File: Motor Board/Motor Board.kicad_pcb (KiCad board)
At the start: 2 copper layers, 37.5 x 39 mm, 30 parts, among them J1 Programmer, J2 Gecko, J3 Gecko, J4 Conn_01x02_Socket, J5 Conn_01x02_Socket, Q1 BSS316NN, U2 PIC18F26K83, U3 MCP2562, U4 INA180, Y1 12MHz Crystal

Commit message: Push motor
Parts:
- added C6: 10uF, Capacitor_SMD:C_0805_2012Metric_Pad1.18x1.45mm_HandSolder, B.Cu at (180.8, 65.3)
- added C7: 10uF, Capacitor_SMD:C_0805_2012Metric_Pad1.18x1.45mm_HandSolder, B.Cu at (171.0, 62.5)
- added C8: 10uF, Capacitor_SMD:C_0805_2012Metric_Pad1.18x1.45mm_HandSolder, B.Cu at (174.0, 62.5)
- added R10: 1kR, Resistor_SMD:R_0805_2012Metric_Pad1.20x1.40mm_HandSolder, B.Cu at (174.0, 56.8)
- added R8: 10kR, Resistor_SMD:R_0805_2012Metric_Pad1.20x1.40mm_HandSolder, B.Cu at (166.9, 65.0)
- added R9: 1kR, Resistor_SMD:R_0805_2012Metric_Pad1.20x1.40mm_HandSolder, B.Cu at (171.0, 56.8)
- added TP1: 5v TP, TestPoint:TestPoint_Pad_1.5x1.5mm, F.Cu at (162.5, 74.5)
- added TP2: PWM TP, TestPoint:TestPoint_Pad_1.5x1.5mm, F.Cu at (162.5, 78.8)
- added TP3: LIM2 TP, TestPoint:TestPoint_Pad_1.5x1.5mm, F.Cu at (165.5, 74.5)
- added TP4: LIM1 TP, TestPoint:TestPoint_Pad_1.5x1.5mm, F.Cu at (165.5, 78.8)
- C1, C2, C3, R1, R2, R3, R4, R6, R7: moved to B.Cu
- F1: value Polyfuse 350mA -> Polyfuse 750mA
- R5: value 62mR -> 10R; moved to B.Cu
- U3, U4, Y1: moved to F.Cu
- moved C1 58.4 mm to (177.7, 55.2), turned to -90 degrees
- moved C2 57.1 mm to (180.8, 55.2), turned to -90 degrees
- moved R2 55.7 mm to (172.8, 49.0), turned to 180 degrees
- moved R1 52.8 mm to (172.8, 45.8), turned to 180 degrees
- moved J4 52.4 mm to (182.0, 48.0)
- moved D2 50.2 mm to (172.8, 45.8), turned to 0 degrees
- moved C3 48.1 mm to (177.7, 60.2), turned to -90 degrees
- moved R5 46.1 mm to (166.9, 60.0), turned to -90 degrees
- moved Y1 45.5 mm to (182.0, 72.5)
- moved R3 43.6 mm to (164.0, 55.0), turned to -90 degrees
- moved R4 43.6 mm to (166.9, 55.0), turned to -90 degrees
- moved R7 43.0 mm to (163.9, 65.0)
- moved Q1 41.6 mm to (172.8, 53.0), turned to 180 degrees
- moved J2 41.4 mm to (186.0, 58.5)
- moved D1 40.9 mm to (172.8, 42.5)
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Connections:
- J3 pad 5: +5V -> Net-(J3-Pin_5)
- J4 pad 1: /LIM_2 -> GND
- J4 pad 2: +5V -> Net-(J4-Pin_2)
- J5 pad 1: /LIM_1 -> GND
- J5 pad 2: +5V -> Net-(J5-Pin_2)
- Q1 pad 2: GND -> +5V
- Q1 pad 3: +5V -> Net-(J3-Pin_5)
- R6 pad 1: /LIM_1 -> +5V
- R6 pad 2: GND -> Net-(J5-Pin_2)
- R7 pad 1: /LIM_2 -> +5V
- R7 pad 2: GND -> Net-(J4-Pin_2)
- U3 pad 2: GND -> Net-(U3-STBY)
- U3 pad 8: GND -> Net-(U3-STBY)
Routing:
- net GND: track 81.2 -> 0.00 mm, vias 6 -> 0
- net Net-(D1-K): track 50.2 -> 0.00 mm, vias 4 -> 0
- net /LIM_1: track 42.4 -> 0.00 mm, vias 2 -> 0
- net /LIM_2: track 40.6 -> 0.00 mm
- net Net-(D2-K): track 38.8 -> 0.00 mm, vias 2 -> 0
- net Net-(D3-K): track 33.1 -> 0.00 mm, vias 2 -> 0
- net +5V: track 31.2 -> 0.00 mm
- net Net-(U4-IN+): track 28.0 -> 0.00 mm, vias 3 -> 0
- net /OSC2: track 28.0 -> 0.00 mm, vias 1 -> 0
- net /OSC1: track 26.5 -> 0.00 mm, vias 1 -> 0
- net Net-(J2-Pin_5): track 20.9 -> 0.00 mm
- net /CANL: track 19.4 -> 0.00 mm, vias 1 -> 0
- net /CANH: track 17.8 -> 0.00 mm, vias 1 -> 0
- net Net-(U2-RA2): track 10.3 -> 0.00 mm
- net /MTR_ON: track 9.39 -> 0.00 mm, vias 1 -> 0
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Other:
- board size 37.5 x 39 mm -> 40 x 40 mm
- board text removed: "CANBUS"
- board text removed: "SERVO"

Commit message: Fix review items
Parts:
- C4, C5, Q1, R1, R2, R3, R4, R6, R7, R8: moved to F.Cu
- F1: value Polyfuse 750mA -> Polyfuse 1.5A
- R5: value 10R -> 50mR
- U3, U4: moved to B.Cu
- moved TP3 30.1 mm to (181.5, 49.0)
- moved TP2 28.2 mm to (171.5, 52.0)
- moved R7 27.4 mm to (181.5, 44.0), turned to 0 degrees
- moved TP4 27.0 mm to (190.0, 67.5)
- moved C6 26.6 mm to (154.5, 69.8)
- moved F1 26.1 mm to (174.5, 68.5), turned to -90 degrees
- moved D1 26.0 mm to (154.5, 61.0), turned to 90 degrees
- moved R1 24.9 mm to (163.2, 68.8), turned to 0 degrees
- moved R2 24.8 mm to (154.5, 65.8), turned to -90 degrees
- moved C2 24.3 mm to (161.2, 69.8)
- moved J5 23.9 mm to (185.6, 61.0), turned to 90 degrees
- moved C1 23.7 mm to (159.0, 69.8)
- moved C3 23.0 mm to (156.8, 69.8), turned to 90 degrees
- moved J2 22.8 mm to (169.2, 74.0), turned to 0 degrees
- moved R6 22.1 mm to (185.5, 65.0), turned to 0 degrees
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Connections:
- C4 pad 2: Net-(C4-Pad2) -> GND
- C5 pad 2: Net-(C4-Pad2) -> GND
- J3 pad 4: /MTR_OUT -> unconnected-(J3-Pin_4-Pad4)
- J4 pad 1: GND -> Net-(J4-Pin_1)
- J4 pad 2: Net-(J4-Pin_2) -> +5V
- J5 pad 1: GND -> Net-(J5-Pin_1)
- J5 pad 2: Net-(J5-Pin_2) -> +5V
- R10 pad 1: GND -> Net-(J5-Pin_1)
- R6 pad 1: +5V -> /LIM_1
- R6 pad 2: Net-(J5-Pin_2) -> GND
- R7 pad 1: +5V -> /LIM_2
- R7 pad 2: Net-(J4-Pin_2) -> GND
- R9 pad 1: GND -> Net-(J4-Pin_1)
- U2 pad 25: /MTR_OUT -> unconnected-(U2-RB4-Pad25)
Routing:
- net GND: track 0.00 -> 92.3 mm, vias 0 -> 1
- net +5V: track 0.00 -> 72.5 mm, vias 0 -> 1
- net /LIM_2: track 0.00 -> 24.8 mm, vias 0 -> 1
- net Net-(U2-RA2): track 0.00 -> 19.3 mm
- net /OSC1: track 0.00 -> 18.6 mm
- net /LIM_1: track 0.00 -> 16.4 mm, vias 0 -> 1
- net Net-(U2-RA1): track 0.00 -> 14.5 mm
- net /CAN_RX: track 0.00 -> 14.1 mm, vias 0 -> 1
- net /OSC2: track 0.00 -> 13.8 mm
- net /MTR_IN: track 0.00 -> 12.2 mm
- net Net-(U2-RA0): track 0.00 -> 11.4 mm
- net Net-(J2-Pin_5): track 0.00 -> 11.0 mm
- net /CANL: track 0.00 -> 10.0 mm
- net /CURR_SENS: track 0.00 -> 9.87 mm, vias 0 -> 1
- net /CANH: track 0.00 -> 9.67 mm
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
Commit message: Forgot to push, fix mosfets
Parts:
- added C1: 0.1uF, Capacitor_SMD:C_0805_2012Metric_Pad1.18x1.45mm_HandSolder, B.Cu at (178.4, 59.4)
- added Q2: DMG2305UX-7, Package_TO_SOT_SMD:SOT-23, B.Cu at (171.1, 53.1)
- added R11: 10kR, Resistor_SMD:R_0805_2012Metric_Pad1.20x1.40mm_HandSolder, B.Cu at (166.8, 55.2)
- added R12: 120R, Resistor_SMD:R_0805_2012Metric_Pad1.20x1.40mm_HandSolder, B.Cu at (167.6, 59.2)
- added R8: 10kR, Resistor_SMD:R_0805_2012Metric_Pad1.20x1.40mm_HandSolder, B.Cu at (176.6, 54.0)
- Q1: footprint Package_TO_SOT_SMD:SOT-323_SC-70 -> Package_TO_SOT_SMD:SOT-323_SC-70_Handsoldering
- moved Q1 0.37 mm to (167.7, 52.0), turned to 0 degrees
- renumbered C3 to C2, C4 to C3, C5 to C4, C6 to C5, C7 to C6, C8 to C7
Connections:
- Q1 pad 1: /MTR_ON -> Net-(Q1-G)
- Q1 pad 2: +5V -> GND
- Q1 pad 3: Net-(J3-Pin_5) -> Net-(Q1-D)
- U3 pad 2: Net-(U3-STBY) -> GND
- U3 pad 8: Net-(U3-STBY) -> GND
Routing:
- net +5V: track 72.5 -> 89.8 mm
- net Net-(Q1-D): track 0.00 -> 13.6 mm, vias 0 -> 1
- net GND: track 92.3 -> 103.6 mm
- net Net-(Q1-G): track 0.00 -> 10.7 mm, vias 0 -> 1
- net Net-(U3-STBY): track 5.48 -> 0.00 mm
- net /MTR_ON: track 6.76 -> 10.4 mm, vias 0 -> 1
- net Net-(J3-Pin_5): track 7.16 -> 10.4 mm
- net /MTR_IN: track 12.2 -> 14.7 mm
- net /ICSPDAT: track 4.25 -> 3.25 mm
- net /ICSPCLK: track 6.13 -> 6.80 mm

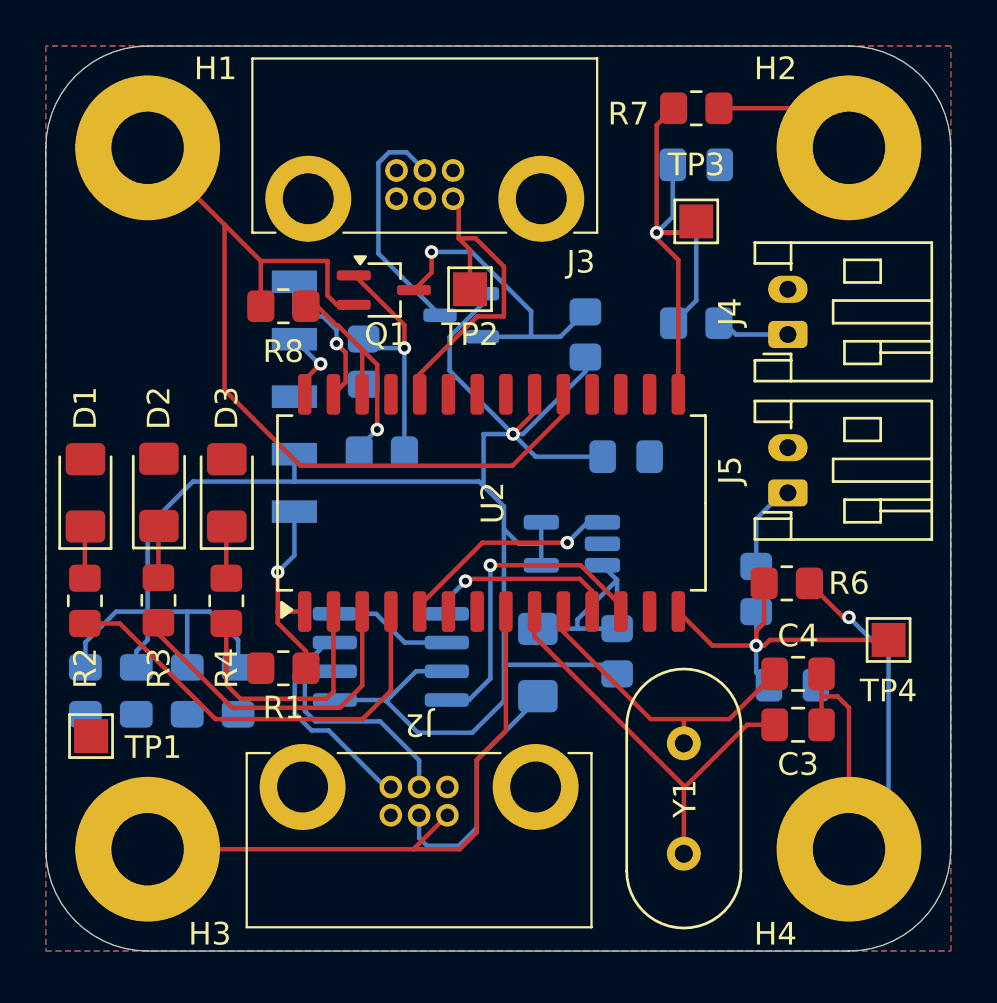
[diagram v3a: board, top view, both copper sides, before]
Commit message: Fix the traces and comments from Pranav
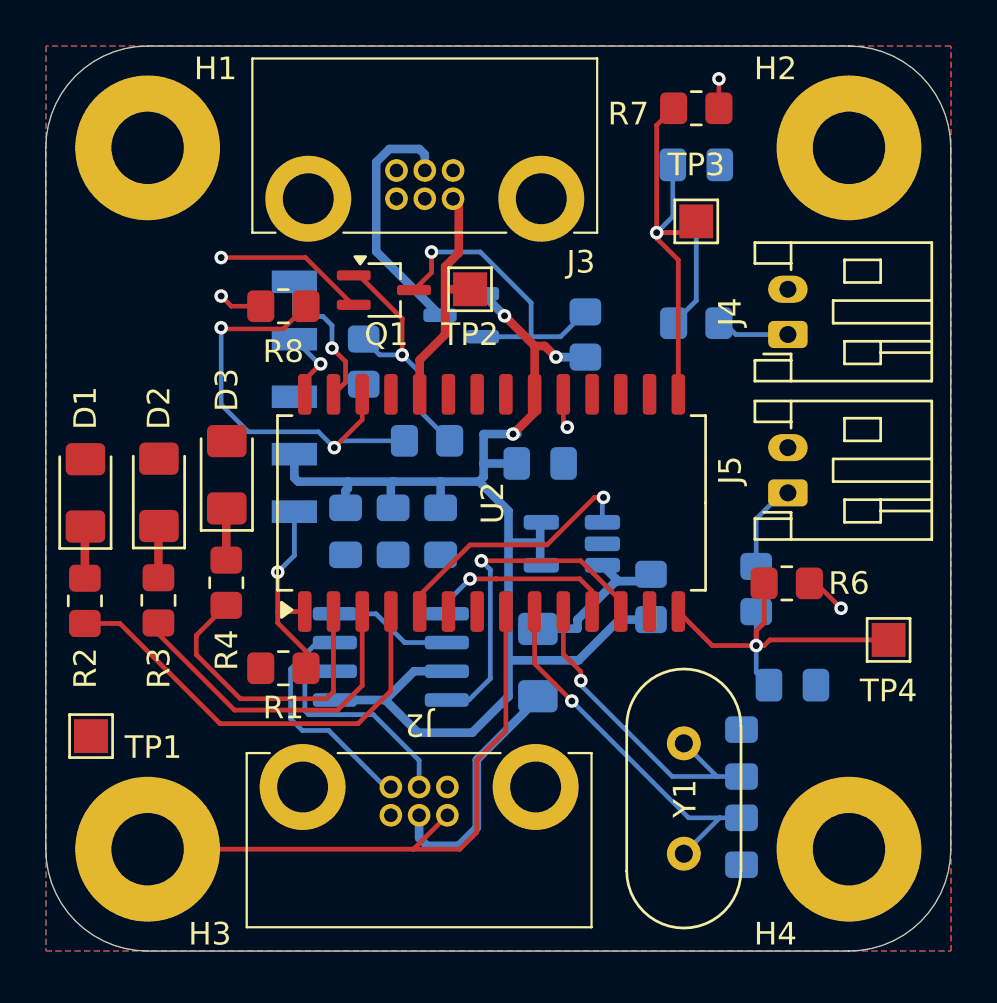
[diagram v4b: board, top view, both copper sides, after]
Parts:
- removed the C2 at (161.2, 69.8)
- C3, C4: moved to B.Cu
- moved C2 20.5 mm to (174.6, 59.7), turned to 180 degrees
- moved C5 13.5 mm to (166.0, 62.7)
- moved C1 11.5 mm to (168.1, 62.7)
- moved C1 8.84 mm to (170.2, 62.7), turned to -90 degrees
- moved C3 5.72 mm to (183.5, 76.4), turned to -90 degrees
- moved C4 4.30 mm to (183.5, 72.5), turned to 90 degrees
- moved R5 2.83 mm to (179.5, 65.6)
- moved R12 2.06 mm to (169.6, 58.7)
- moved D3 0.80 mm to (160.8, 60.2)
- moved R4 0.80 mm to (160.7, 65.0)
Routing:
- net GND: track 103.6 -> 46.1 mm, vias 1 -> 5
- net +5V: track 89.8 -> 60.8 mm, vias 1 -> 3
- net /MTR_ON: track 10.4 -> 19.5 mm, vias 1 -> 2
- net /MTR_IN: track 14.7 -> 10.6 mm
- net Net-(U4-IN+): track 9.45 -> 7.19 mm
- net /OSC1: track 18.6 -> 16.5 mm, vias 0 -> 1
- net Net-(U2-RA0): track 11.4 -> 13.3 mm
- net /CURR_SENS: track 9.87 -> 11.8 mm
- net /OSC2: track 13.8 -> 15.3 mm, vias 0 -> 1
- net /CAN_RX: track 14.1 -> 15.1 mm
- net Net-(J3-Pin_5): track 10.4 -> 11.1 mm
- net /CANH: track 9.67 -> 10.3 mm
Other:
- board text added: "MCLR"

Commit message: redit layout
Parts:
- removed the C1 at (168.1, 62.7)
- removed the C1 at (170.2, 62.7)
- removed the R8 at (163.2, 52.8)
- removed the R8 at (176.6, 54.0)
- added C1: 0.1uF, Capacitor_SMD:C_0805_2012Metric_Pad1.18x1.45mm_HandSolder, F.Cu at (176.9, 63.2)
- added G***: LOGO, Team_Logo:Logo_Horizontal_Silkscreen_10mm, B.Cu at (174.5, 67.8)
- added R8: 10kR, Resistor_SMD:R_0805_2012Metric_Pad1.20x1.40mm_HandSolder, B.Cu at (169.2, 55.5)
- C2, C3, C4, C5, C6, C7, F1, R10, R5, R9, U3, U4: moved to F.Cu
- J1: footprint Canhw:PinSocket_5x2.54_SMD_90deg_952-3198-1-ND -> canhw:PinSocket_5x2.54_SMD_90deg_952-3198-1-ND
- J2, J3: footprint Canhw:connector_Harwin_G125–MG10605M4P -> canhw:connector_Harwin_G125–MG10605M4P
- Q1, R1: moved to B.Cu
- Y1: value 12MHz Crystal -> 12MHz Crystal
- moved TP1 38.2 mm to (180.0, 43.1), turned to 180 degrees
- moved C3 30.7 mm to (155.2, 64.5), turned to 90 degrees
- moved C4 28.5 mm to (155.2, 68.8), turned to -90 degrees
- moved Y1 25.2 mm to (159.3, 64.1), turned to -90 degrees
- moved C2 19.6 mm to (191.3, 70.0), turned to -90 degrees
- moved R4 13.2 mm to (161.0, 51.8), turned to 0 degrees
- moved U4 13.1 mm to (187.5, 69.6), turned to -90 degrees
- moved R7 12.1 mm to (179.3, 55.9), turned to -90 degrees
- moved R3 11.4 mm to (161.0, 54.9), turned to 0 degrees
- moved C7 11.1 mm to (179.3, 60.4), turned to 90 degrees
- moved D3 10.4 mm to (155.7, 51.1), turned to 180 degrees
- moved R2 10.2 mm to (161.1, 57.9), turned to 0 degrees
- moved TP2 9.96 mm to (180.0, 46.7)
- moved U3 9.35 mm to (164.6, 77.0), turned to -90 degrees
- moved C5 9.06 mm to (165.6, 71.8), turned to 180 degrees
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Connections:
- U2 pad 14: /LIM_1 -> unconnected-(U2-RC3-Pad14)
- U2 pad 15: /LIM_2 -> unconnected-(U2-RC4-Pad15)
- U2 pad 16: unconnected-(U2-RC5-Pad16) -> /CURR_SENS
- U2 pad 22: unconnected-(U2-RB1-Pad22) -> /LIM_1
- U2 pad 23: unconnected-(U2-RB2-Pad23) -> /LIM_2
- U2 pad 5: /CURR_SENS -> unconnected-(U2-RA3-Pad5)
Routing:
- net GND: track 46.1 -> 24.2 mm, vias 5 -> 29
- net +5V: track 60.8 -> 39.5 mm, vias 3 -> 8
- net Net-(U2-RA2): track 19.5 -> 3.24 mm
- net /MTR_ON: track 19.5 -> 3.65 mm, vias 2 -> 1
- net /MTR_IN: track 10.6 -> 22.8 mm, vias 0 -> 2
- net Net-(U2-RA1): track 14.6 -> 2.64 mm
- net /~{MCLR}: track 8.94 -> 19.2 mm
- net Net-(U2-RA0): track 13.3 -> 3.38 mm
- net /LIM_2: track 24.8 -> 15.8 mm, vias 1 -> 0
- net /ICSPCLK: track 6.80 -> 14.5 mm
- net /ICSPDAT: track 3.25 -> 10.5 mm
- net /CANL: track 10.0 -> 17.0 mm
- net Net-(Q1-D): track 13.8 -> 7.23 mm, vias 1 -> 0
- net Net-(Q1-G): track 11.2 -> 5.90 mm, vias 1 -> 0
- net /CAN_TX: track 8.49 -> 13.6 mm, vias 1 -> 0
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- added copper zone on F.Cu, net GND
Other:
- board size 40 x 40 mm -> 40.2 x 40.4 mm
- board text added: "+5V"
- board text added: "CAN"
- board text added: "LIM1"
- board text added: "LIM2"
- board text added: "MTR"
- board text added: "Motor Board Connor Stubbs 24-05-2024"
- board text added: "~{MCLR}"
- board text removed: "MCLR"

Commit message: implemented Joes changes
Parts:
- moved J2 0.38 mm to (176.3, 74.3)
- moved D1 0.13 mm to (155.8, 57.9)
- moved D2 0.13 mm to (155.8, 54.5)
- moved D3 0.13 mm to (155.8, 51.1)
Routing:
- net /CANL: track 17.0 -> 16.5 mm
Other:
- board text added: "Fast Fourier Board Motor Board Connor Stubbs 24-05-2024"
- board text removed: "Motor Board Connor Stubbs 24-05-2024"

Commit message: Final PCB touches; gerbs
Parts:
- moved C2 0.90 mm to (190.4, 69.8)
- moved C5 0.64 mm to (165.1, 72.1), turned to 0 degrees
- moved J3 0.39 mm to (169.9, 47.9)
- moved J2 0.39 mm to (176.3, 74.7)
- moved C1 0.13 mm to (176.8, 63.2)
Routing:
- net +5V: track 39.5 -> 30.7 mm
- net GND: track 24.2 -> 27.6 mm
- net /CANH: track 14.0 -> 12.8 mm
- net Net-(J3-Pin_5): track 7.75 -> 8.49 mm
